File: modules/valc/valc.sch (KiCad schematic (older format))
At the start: 29 parts, among them J1 2, J10 11, J11 12, J12 13, J13 A0, J14 A1, J15 A2, J16 A3, J17 A4, J18 A5, J19 Vcc, J2 3, J20 Gnd, J3 4, J4 5, J5 6, J6 7, J7 8, J8 9, J9 10, SW1001 Rotary_Encoder_Switch

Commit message: Valcoder in work
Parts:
- removed D1003: 6x6-tact-btn, CommonLibrary:6x6-tact-btn, symbol CommonLibrary:6x6-tact-btn
- added C1, C2: 4.7nF, Capacitor_SMD:C_0805_2012Metric_Pad1.15x1.40mm_HandSolder, symbol Device:C
- added C3: C, Capacitor_SMD:C_0805_2012Metric_Pad1.15x1.40mm_HandSolder, symbol Device:C
- added D1, D2, D3, D4: LL4148, Diode_SMD:D_MiniMELF, symbol Diode:LL4148
- added R1, R2, R3, R4: 5k, Resistor_SMD:R_0805_2012Metric_Pad1.15x1.40mm_HandSolder, symbol Device:R
- added R5: 10k, Resistor_SMD:R_0805_2012Metric_Pad1.15x1.40mm_HandSolder, symbol Device:R
- added U1: 74LS139, Package_SO:SOIC-16_3.9x9.9mm_P1.27mm, symbol 74xx_IEEE:74LS139
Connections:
- net at J11.1 (Pin_1): now also U1.2 (A)
- net VCC: now reaches J19.1 (Pin_1)
- net VCC: now also C3.1, R1.1, R3.1, R5.1, U1.16 (VCC)
- net GND: now reaches J20.1 (Pin_1)
- net GND: now also SW1001.C, C1.2, C2.2, C3.2, U1.1 (~EN), U1.8 (GND)
- net at J12.1 (Pin_1): now also U1.3 (B)
- net at SW1001.A: now also R3.2, R4.1
- net at SW1001.B: now also R1.2, R2.1
- net at SW1001.S1: now also D1001.2, D1002.2, D1004.2, R5.2
- net at SW1001.S2: now also D1.2 (A)
- net at D1004.1: now also D2.2 (A)
- net at D1001.1: now also D3.2 (A)
- net at D1002.1: now also D4.2 (A)
- new net: D1.1 (K), U1.4 (~Q0)
- new net: D2.1 (K), U1.5 (~Q1)
- new net: D3.1 (K), U1.6 (~Q2)
- new net: D4.1 (K), U1.7 (~Q3)
- new net: C2.1, R4.2
- new net: C1.1, R2.2
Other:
- moved on the sheet: D1001, D1002, D1004, SW1001

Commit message: Valcoder pcb ready
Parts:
- added R6: 5k, Resistor_SMD:R_0805_2012Metric_Pad1.15x1.40mm_HandSolder, symbol Device:R
- added unit 2 of U1
- C3: value C -> 0,1uF
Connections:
- net GND: now also U1.8 (GND)
- net VCC: now also R6.1, U1.16 (VCC)
- net at J13.1 (Pin_1): now also C1.1, R2.2
- net at J14.1 (Pin_1): now also C2.1, R4.2
- net at J15.1 (Pin_1): now also D1001.2, D1002.2, D1004.2, R5.2, SW1001.S1
- new net: R6.2, U1.13 (B), U1.14 (A), U1.15 (~EN)
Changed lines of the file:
@@
 	3650 1450 3650 1525
 Wire Wire Line
-	3650 1925 3650 2100
+	3650 1925 3650 2025
 Wire Wire Line
 	3650 2400 3650 2500
@@
 	4900 1450 4900 1525
 Wire Wire Line
-	4900 1925 4900 2100
+	4900 1925 4900 2025
 Wire Wire Line
 	4900 2400 4900 2500
@@
 P 6000 1900
 F 0 "C3" H 6115 1946 50  0000 L CNN
-F 1 "C" H 6115 1855 50  0000 L CNN
+F 1 "0,1uF" H 6115 1855 50  0000 L CNN
 F 2 "Capacitor_SMD:C_0805_2012Metric_Pad1.15x1.40mm_HandSolder" H 6038 1750 50  0001 C CNN
 F 3 "~" H 6000 1900 50  0001 C CNN
@@
 Wire Wire Line
 	6000 2050 6000 2175
+Wire Wire Line
+	4900 2025 5650 2025
+Connection ~ 4900 2025
+Wire Wire Line
+	4900 2025 4900 2100
+Wire Wire Line
+	3650 2025 3250 2025
+Wire Wire Line
+	3250 2025 3250 575
+Wire Wire Line
+	3250 575  6500 575
+Wire Wire Line
+	6500 575  6500 2500
+Connection ~ 3650 2025
+Wire Wire Line
+	3650 2025 3650 2100
+Wire Wire Line
+	4900 3000 4900 2800
+Wire Wire Line
+	4900 2800 6750 2800
+$Comp
+L power:VCC #PWR012
+U 1 1 5D8B7FB8
+P 5500 4200
+F 0 "#PWR012" H 5500 4050 50  0001 C CNN
+F 1 "VCC" H 5517 4373 50  0000 C CNN
+F 2 "" H 5500 4200 50  0001 C CNN
+F 3 "" H 5500 4200 50  0001 C CNN
+	1    5500 4200
+	1    0    0    -1
+$EndComp
+$Comp
+L Device:R R6
+U 1 1 5D8B86A9
+P 5500 4425
+F 0 "R6" H 5570 4471 50  0000 L CNN
+F 1 "5k" H 5570 4380 50  0000 L CNN
+F 2 "Resistor_SMD:R_0805_2012Metric_Pad1.15x1.40mm_HandSolder" V 5430 4425 50  0001 C CNN
+F 3 "~" H 5500 4425 50  0001 C CNN
+	1    5500 4425
+	1    0    0    -1
+$EndComp
+Wire Wire Line
+	5500 4200 5500 4275
+$Comp
+L 74xx_IEEE:74LS139 U1
+U 2 1 5D8C26BB
+P 6050 4900
+F 0 "U1" H 6050 5516 50  0000 C CNN
+F 1 "74LS139" H 6050 5425 50  0000 C CNN
+F 2 "Package_SO:SOIC-16_3.9x9.9mm_P1.27mm" H 6050 4900 50  0001 C CNN
+F 3 "" H 6050 4900 50  0001 C CNN
+	2    6050 4900
+	1    0    0    -1
+$EndComp
+Wire Wire Line
+	5500 4575 5500 4650
+Wire Wire Line
+	5500 4800 5500 4650
+Connection ~ 5500 4650
+Wire Wire Line
+	5500 5150 5500 4800
+Connection ~ 5500 4800
+Wire Wire Line
+	6750 2500 6500 2500
+Wire Wire Line
+	5650 2650 6750 2650
+Wire Wire Line
+	5650 2025 5650 2650
 $EndSCHEMATC

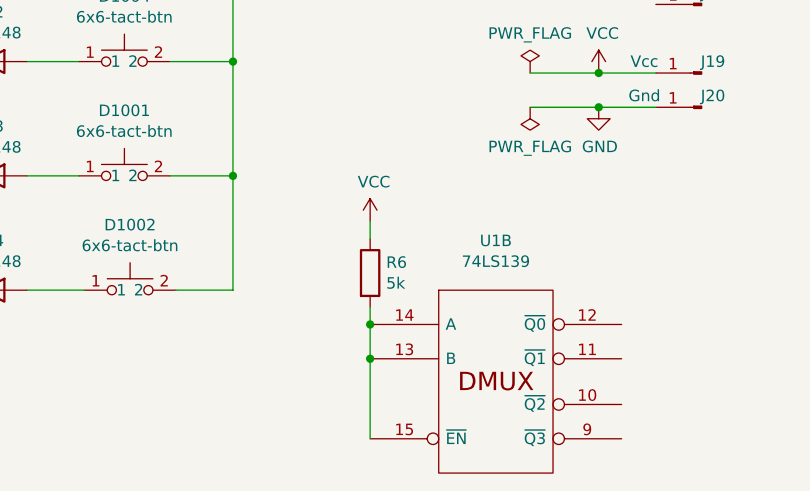
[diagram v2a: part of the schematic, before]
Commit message: Fix pullup
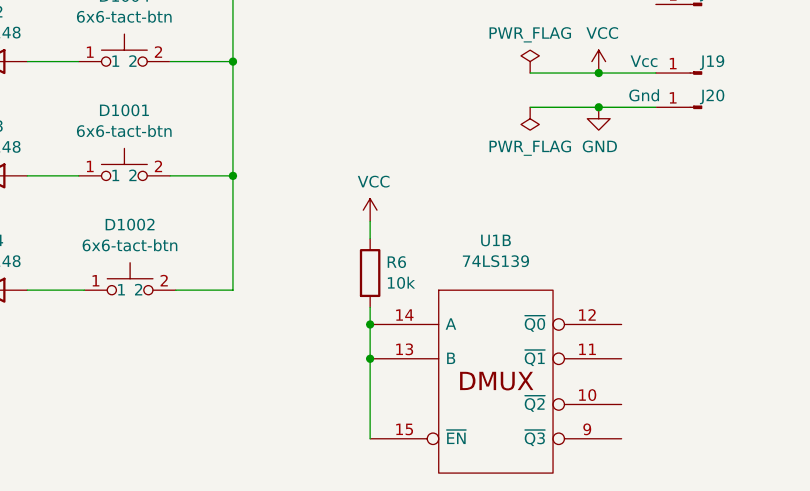
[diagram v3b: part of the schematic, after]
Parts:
- R6: value 5k -> 10k
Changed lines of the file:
@@
 P 5500 4425
 F 0 "R6" H 5570 4471 50  0000 L CNN
-F 1 "5k" H 5570 4380 50  0000 L CNN
+F 1 "10k" H 5570 4380 50  0000 L CNN
 F 2 "Resistor_SMD:R_0805_2012Metric_Pad1.15x1.40mm_HandSolder" V 5430 4425 50  0001 C CNN
 F 3 "~" H 5500 4425 50  0001 C CNN

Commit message: Valcoder polishing
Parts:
- renumbered D1004 to D2, D1001 to D3, D1002 to D4, SW1001 to SW1, D1 to VD1, D2 to VD2, D3 to VD3, D4 to VD4
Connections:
- no-connect marks 0 -> 18
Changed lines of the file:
@@
 $EndComp
 $Comp
-L Device:Rotary_Encoder_Switch SW1001
+L Device:Rotary_Encoder_Switch SW1
 U 1 1 5D7E7CAC
 P 4275 2450
-F 0 "SW1001" H 4250 2200 50  0000 C CNN
+F 0 "SW1" H 4250 2200 50  0000 C CNN
 F 1 "Rotary_Encoder_Switch" H 4275 2726 50  0000 C CNN
 F 2 "Rotary_Encoder:RotaryEncoder_Alps_EC11E-Switch_Vertical_H20mm" H 4125 2610 50  0001 C CNN
@@
 $EndComp
 $Comp
-L CommonLibrary:6x6-tact-btn D1004
+L CommonLibrary:6x6-tact-btn D2
 U 1 1 5D7E8B22
 P 4425 3500
-F 0 "D1004" H 4425 3785 50  0000 C CNN
+F 0 "D2" H 4425 3785 50  0000 C CNN
 F 1 "6x6-tact-btn" H 4425 3694 50  0000 C CNN
 F 2 "CommonLibrary:6x6-tact-btn" H 4425 3600 50  0001 C CNN
@@
 $EndComp
 $Comp
-L CommonLibrary:6x6-tact-btn D1001
+L CommonLibrary:6x6-tact-btn D3
 U 1 1 5D7E8F4B
 P 4425 4000
-F 0 "D1001" H 4425 4285 50  0000 C CNN
+F 0 "D3" H 4425 4285 50  0000 C CNN
 F 1 "6x6-tact-btn" H 4425 4194 50  0000 C CNN
 F 2 "CommonLibrary:6x6-tact-btn" H 4425 4100 50  0001 C CNN
@@
 $EndComp
 $Comp
-L CommonLibrary:6x6-tact-btn D1002
+L CommonLibrary:6x6-tact-btn D4
 U 1 1 5D7E95C4
 P 4450 4500
-F 0 "D1002" H 4450 4785 50  0000 C CNN
+F 0 "D4" H 4450 4785 50  0000 C CNN
 F 1 "6x6-tact-btn" H 4450 4694 50  0000 C CNN
 F 2 "CommonLibrary:6x6-tact-btn" H 4450 4600 50  0001 C CNN
@@
 $EndComp
 $Comp
-L Diode:LL4148 D1
+L Diode:LL4148 VD1
 U 1 1 5D89E207
 P 3850 3000
-F 0 "D1" H 3850 3216 50  0000 C CNN
+F 0 "VD1" H 3850 3216 50  0000 C CNN
 F 1 "LL4148" H 3850 3125 50  0000 C CNN
 F 2 "Diode_SMD:D_MiniMELF" H 3850 2825 50  0001 C CNN
@@
 $EndComp
 $Comp
-L Diode:LL4148 D2
+L Diode:LL4148 VD2
 U 1 1 5D89E9E4
 P 3850 3500
-F 0 "D2" H 3850 3716 50  0000 C CNN
+F 0 "VD2" H 3850 3716 50  0000 C CNN
 F 1 "LL4148" H 3850 3625 50  0000 C CNN
 F 2 "Diode_SMD:D_MiniMELF" H 3850 3325 50  0001 C CNN
@@
 $EndComp
 $Comp
-L Diode:LL4148 D3
+L Diode:LL4148 VD3
 U 1 1 5D89EEED
 P 3850 4000
-F 0 "D3" H 3850 4216 50  0000 C CNN
+F 0 "VD3" H 3850 4216 50  0000 C CNN
 F 1 "LL4148" H 3850 4125 50  0000 C CNN
 F 2 "Diode_SMD:D_MiniMELF" H 3850 3825 50  0001 C CNN
@@
 $EndComp
 $Comp
-L Diode:LL4148 D4
+L Diode:LL4148 VD4
 U 1 1 5D89F449
 P 3850 4500
-F 0 "D4" H 3850 4716 50  0000 C CNN
+F 0 "VD4" H 3850 4716 50  0000 C CNN
 F 1 "LL4148" H 3850 4625 50  0000 C CNN
 F 2 "Diode_SMD:D_MiniMELF" H 3850 4325 50  0001 C CNN
@@
 Wire Wire Line
 	5650 2025 5650 2650
+NoConn ~ 1225 2500
+NoConn ~ 1225 2650
+NoConn ~ 1225 2800
+NoConn ~ 1225 2950
+NoConn ~ 1225 3100
+NoConn ~ 1225 3250
+NoConn ~ 1225 3400
+NoConn ~ 1225 3550
+NoConn ~ 1225 3700
+NoConn ~ 1225 3850
+NoConn ~ 6750 2950
+NoConn ~ 6750 3100
+NoConn ~ 6750 3250
+NoConn ~ 6025 3425
+NoConn ~ 6600 4650
+NoConn ~ 6600 4800
+NoConn ~ 6600 5000
+NoConn ~ 6600 5150
 $EndSCHEMATC
